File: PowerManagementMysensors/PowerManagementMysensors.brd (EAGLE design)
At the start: 49.5 x 44.1 mm, 51 parts, among them IC2 AT25DF512C-SSHN-B, U1 LM8364BALMF20, U2 SI2399DS-T1-GE3, U3 SI2399DS-T1-GE3, U4 MCP1640BT-I/CHY, U5 TPS61222DCKT

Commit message: jst connector added
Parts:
- BATT: value M02PTH -> (none); device SparkFun-Connectors:1X02 -> adafruit:JST-PH-2-THM
- J10: device SparkFun-Connectors:1X05 -> SparkFun-Connectors:1X04
- J7: device SparkFun-Connectors:1X07 -> SparkFun-Connectors:1X05
- J8: device SparkFun-Connectors:1X04 -> SparkFun-Connectors:1X05
- J9: device SparkFun-Connectors:1X05 -> SparkFun-Connectors:1X07
- moved J3 17.8 mm to (47.6, 36.8)
- moved J8 16.3 mm to (37.5, 24.1), turned to 0 degrees
- moved J10 11.4 mm to (47.6, 19.1), turned to 180 degrees
- moved J7 7.18 mm to (37.5, 26.7)
- moved J9 7.18 mm to (32.4, 21.6)
- moved BATT 0.45 mm to (46.8, 4.65), turned to 90 degrees
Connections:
- net GND: now also J7.3, J9.5; no longer J7.5, J9.3
- net INT1: now also J10.4; no longer J3.4
- net INT2: now also J3.4; no longer J8.4
- net MISO: now also J9.4; no longer J7.4
- net MOSI: now also J9.3; no longer J7.3
- net SCK: now also J9.2; no longer J7.2
- net SCL: now also J7.1, J8.1; no longer J10.1, J9.1
- net SDA: now also J7.2, J8.2; no longer J10.2, J9.2
- net SPI_CSN: now also J9.1; no longer J7.1
- net V+5: now also J10.1, J7.5, J8.5, J9.7; no longer J10.5, J7.7, J8.1, J9.5
- net VCC_SENSORS: now also J10.2, J7.4, J8.4, J9.6; no longer J10.4, J7.6, J8.2, J9.4
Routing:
- net EN_BOOST: track 64.2 -> 65.6 mm
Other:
- board text removed: "VBAT"

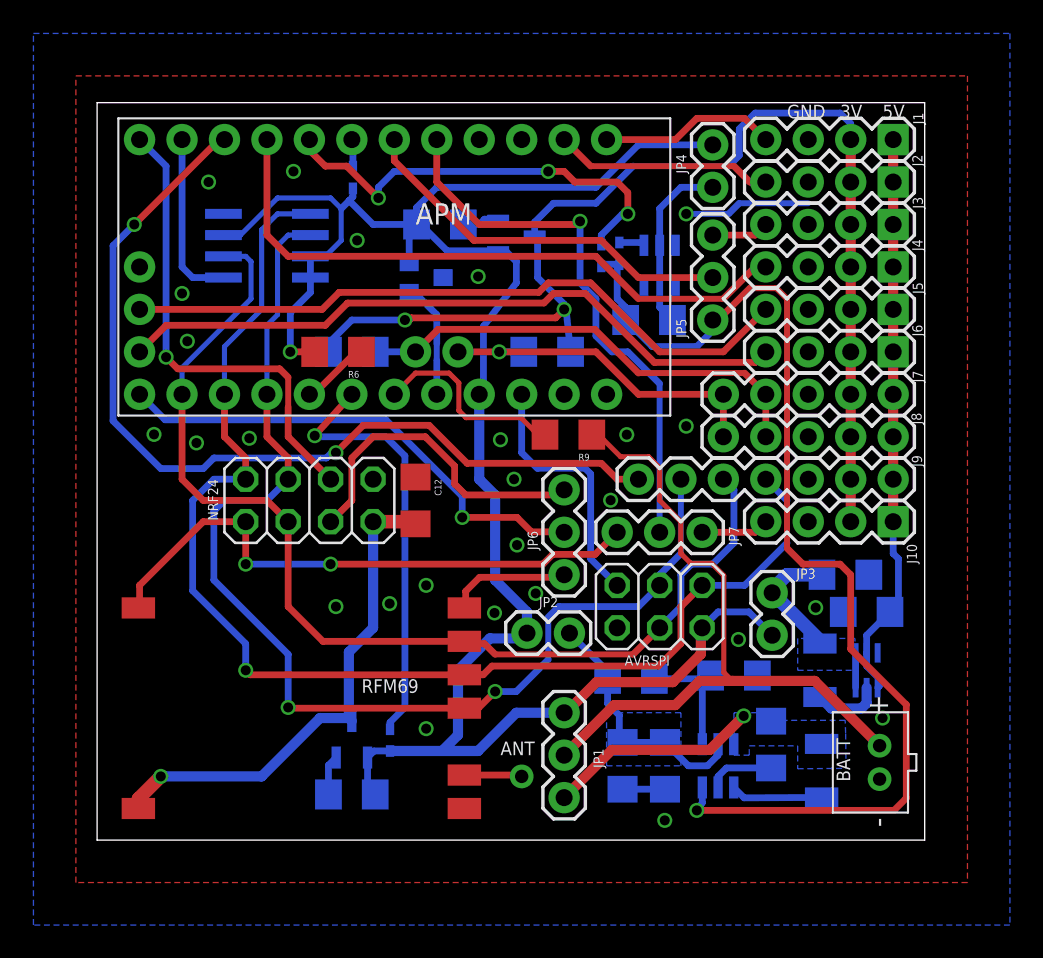
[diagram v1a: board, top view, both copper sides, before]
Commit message: changes
-res + zener to flash mem avoid fry
- dual schottky instead two single
- minor component ref changes
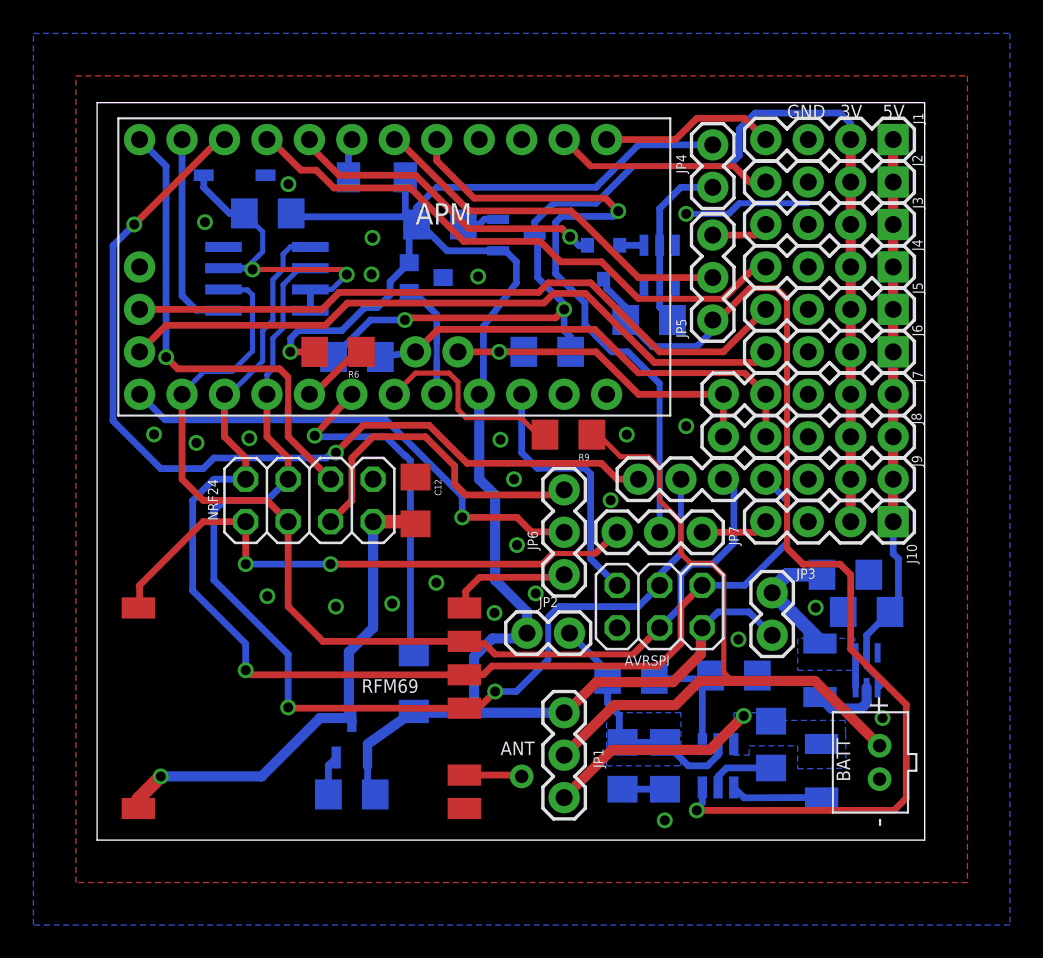
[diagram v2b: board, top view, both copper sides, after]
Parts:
- removed D4, D5: RB520S30T1G, diode:SOD523
- added D2: LL103A-GS08TR-ND, semicon-smd-ipc:SOD80
- added D6: BAT54C, zetex:SOT-23
- added R10: 47r-100r, SparkFun-Passives:1206
- D1: value RB520S30T1G -> LL103A-GS08TR-ND; device diode:SOD523 -> semicon-smd-ipc:SOD80
- D3: value RB520S30T1G -> BZT52H-B3V6; device diode:SOD523 -> adafruit:SOD-123
- moved D3 23.5 mm to (8.23, 39.8), turned to 180 degrees
- moved D1 14.2 mm to (16.7, 39.6), turned to 180 degrees
- moved IC2 1.98 mm to (10.2, 33.6)
- moved R8 0.43 mm to (15.5, 28.9)
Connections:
- new net D5_ENBOOST: APM.5, D6.3
- net EN_BOOST: now also D6.1; no longer D1.C, D3.C
- net EN_POWER: now also D1.1; no longer D5.C
- net EN_POWERRF: now also D2.1; no longer D4.C
- net GND: now also D3.A
- net N$5: now also D6.2; no longer D3.A
- net N$6: now also D3.C, IC2.3, IC2.7, IC2.8, R10.1; no longer APM.5, D1.A
- net VCC: now also D1.2, D2.2, R10.2; no longer D4.A, D5.A, IC2.3, IC2.7, IC2.8
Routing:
- net D5_ENBOOST: track 0.00 -> 19.5 mm, vias 0 -> 1
- net N$6: track 26.4 -> 19.2 mm, vias 3 -> 2
- net VCC: track 121.9 -> 115.8 mm
- net D2: track 33.4 -> 39.1 mm
- net EN_POWERRF: track 25.9 -> 21.3 mm
- net PWM: track 37.9 -> 34.6 mm
- net SCK: track 69.5 -> 67.1 mm
- net MISO: track 76.3 -> 74.0 mm
- net FLASH_CSN: track 10.4 -> 12.2 mm
- net EN_BOOST: track 65.6 -> 63.8 mm
- net MOSI: track 65.0 -> 64.2 mm
- net EN_POWER: track 1.65 -> 2.43 mm
- net D3: track 23.2 -> 22.5 mm
- net GND: vias 26 -> 25

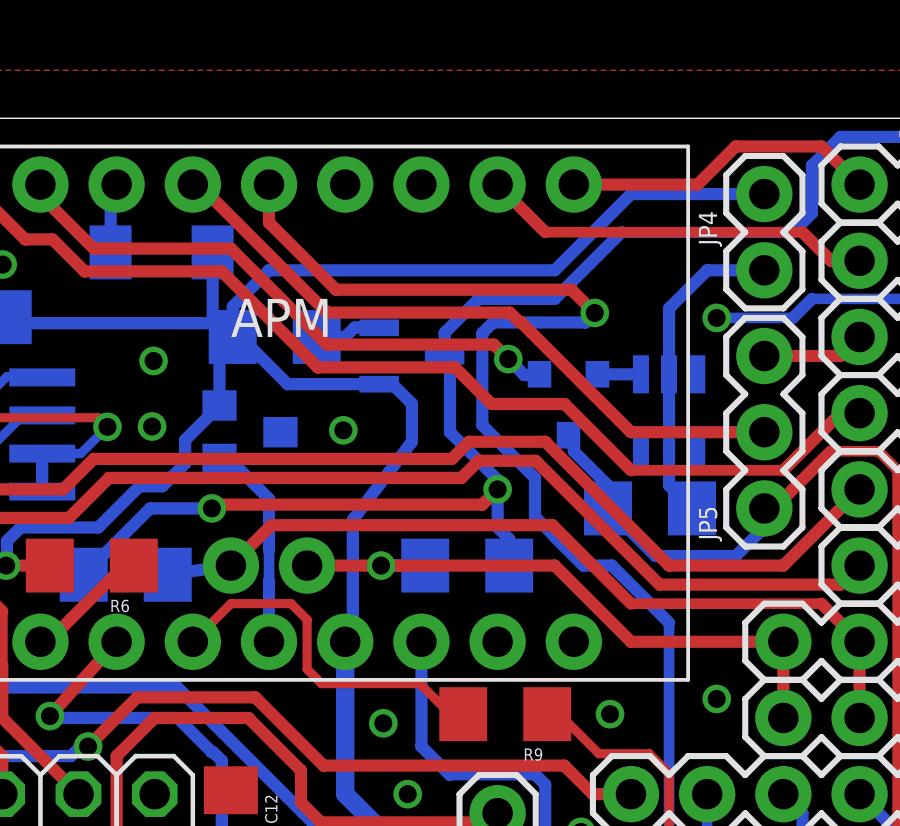
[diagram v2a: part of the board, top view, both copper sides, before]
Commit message: rst pin on arduino pro mini connected
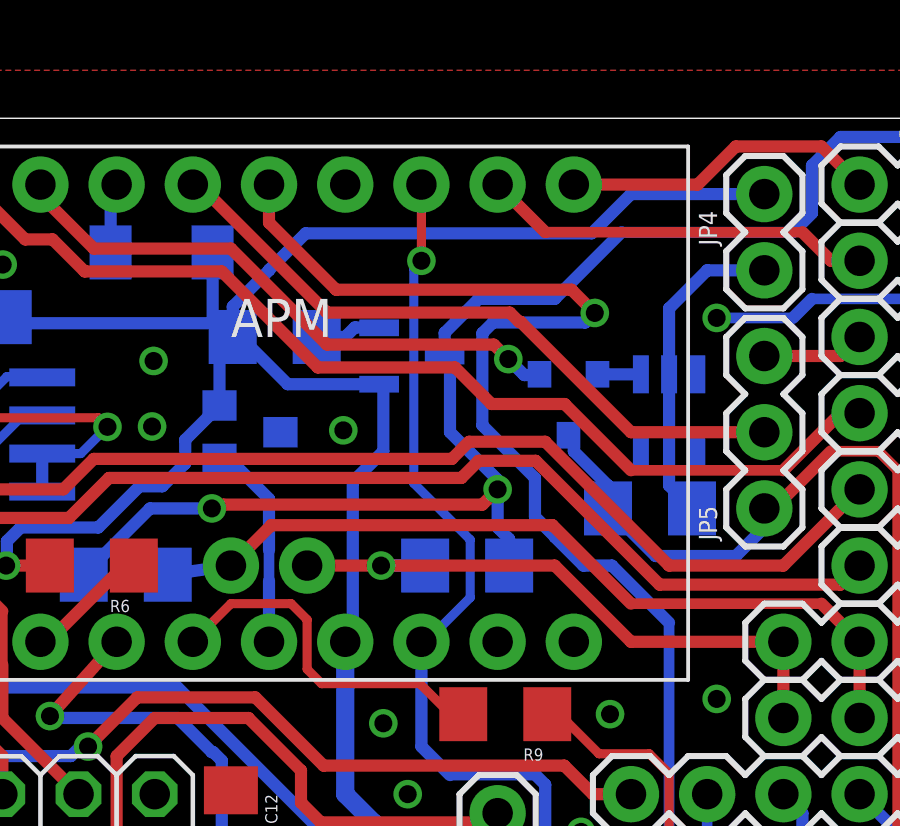
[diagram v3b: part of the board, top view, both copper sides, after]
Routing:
- net RST: track 15.5 -> 32.4 mm, vias 0 -> 1
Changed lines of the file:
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@@
 <wire x1="18.669" y1="36.3885" x2="19.1105" y2="36.83" width="0.4064" layer="16"/>
 <wire x1="19.1105" y1="36.83" x2="19.1105" y2="37.843" width="0.4064" layer="16"/>
-<wire x1="23.114" y1="30.734" x2="25.0825" y2="33.3375" width="0.4064" layer="16"/>
-<wire x1="25.0825" y1="33.3375" x2="25.0825" y2="34.6075" width="0.4064" layer="16"/>
-<wire x1="25.0825" y1="34.6075" x2="24.4475" y2="35.2425" width="0.4064" layer="16"/>
 <wire x1="24.4475" y1="35.2425" x2="24.003" y2="35.2425" width="0.4064" layer="16"/>
 <wire x1="24.003" y1="35.2425" x2="23.9903" y2="35.2552" width="0.4064" layer="16"/>
@@
 <wire x1="19.428" y1="36.5125" x2="19.1105" y2="36.83" width="0.4064" layer="16"/>
 <wire x1="19.1105" y1="37.843" x2="20.32" y2="39.0525" width="0.4064" layer="16"/>
-<wire x1="20.32" y1="39.0525" x2="29.845" y2="39.0525" width="0.4064" layer="16"/>
-<wire x1="29.845" y1="39.0525" x2="32.385" y2="41.5925" width="0.4064" layer="16"/>
 <wire x1="25.7175" y1="12.3825" x2="25.7175" y2="13.6525" width="0.6096" layer="16"/>
 <wire x1="25.7175" y1="13.6525" x2="23.8125" y2="15.5575" width="0.6096" layer="16"/>
 <wire x1="23.8125" y1="15.5575" x2="23.8125" y2="20.6375" width="0.6096" layer="16"/>
 <wire x1="23.8125" y1="20.6375" x2="22.86" y2="21.59" width="0.6096" layer="16"/>
-<wire x1="23.114" y1="26.924" x2="23.114" y2="30.734" width="0.4064" layer="16"/>
+<wire x1="23.114" y1="26.924" x2="23.114" y2="32.004" width="0.4064" layer="16"/>
 <wire x1="27.94" y1="7.62" x2="28.0416" y2="7.62" width="0.6096" layer="1"/>
 <wire x1="28.0416" y1="7.62" x2="29.8704" y2="9.4488" width="0.6096" layer="1"/>
@@
 <wire x1="17.526" y1="32.6136" x2="17.526" y2="33.401" width="0.4064" layer="16"/>
 <wire x1="17.526" y1="33.401" x2="18.669" y2="34.544" width="0.4064" layer="16"/>
+<wire x1="23.114" y1="32.004" x2="24.13" y2="33.02" width="0.4064" layer="16"/>
+<wire x1="24.13" y1="33.02" x2="24.13" y2="35.1155" width="0.4064" layer="16"/>
+<wire x1="24.13" y1="35.1155" x2="23.9903" y2="35.2552" width="0.4064" layer="16"/>
+<wire x1="20.32" y1="39.0525" x2="20.32" y2="39.0652" width="0.4064" layer="16"/>
+<wire x1="20.32" y1="39.0652" x2="21.5392" y2="40.2844" width="0.4064" layer="16"/>
+<wire x1="21.5392" y1="40.2844" x2="31.0769" y2="40.2844" width="0.4064" layer="16"/>
+<wire x1="31.0769" y1="40.2844" x2="32.385" y2="41.5925" width="0.4064" layer="16"/>
 </signal>
 <signal name="N$1">
@@
 <wire x1="26.3525" y1="22.225" x2="25.4" y2="23.1775" width="0.4064" layer="16"/>
 <wire x1="25.4" y1="23.1775" x2="25.4" y2="26.67" width="0.4064" layer="16"/>
-<wire x1="25.4" y1="26.67" x2="25.4" y2="41.91" width="0" layer="19" extent="1-1"/>
+<wire x1="25.4" y1="26.67" x2="25.5524" y2="26.67" width="0.3048" layer="16"/>
+<wire x1="25.5524" y1="26.67" x2="27.0256" y2="28.1432" width="0.3048" layer="16"/>
+<wire x1="27.0256" y1="28.1432" x2="27.0256" y2="30.0736" width="0.3048" layer="16"/>
+<wire x1="27.0256" y1="30.0736" x2="25.146" y2="31.9532" width="0.3048" layer="16"/>
+<wire x1="25.146" y1="31.9532" x2="25.146" y2="39.116" width="0.3048" layer="16"/>
+<wire x1="25.146" y1="39.116" x2="25.4" y2="39.37" width="0.3048" layer="16"/>
+<via x="25.4" y="39.37" extent="1-16" drill="0.6" shape="square"/>
+<wire x1="25.4" y1="39.37" x2="25.4" y2="41.91" width="0.3048" layer="1"/>
 </signal>
 <signal name="TX">
